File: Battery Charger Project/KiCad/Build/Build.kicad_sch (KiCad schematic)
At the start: 21 parts, among them J1 Screw_Terminal_01x03, J2 Screw_Terminal_01x03, J3 Screw_Terminal_01x02, J5 726386-2, J6 726386-2, J9 726386-2, U1 LAUNCHXL-F28379D, U2 TMCS1133C3A

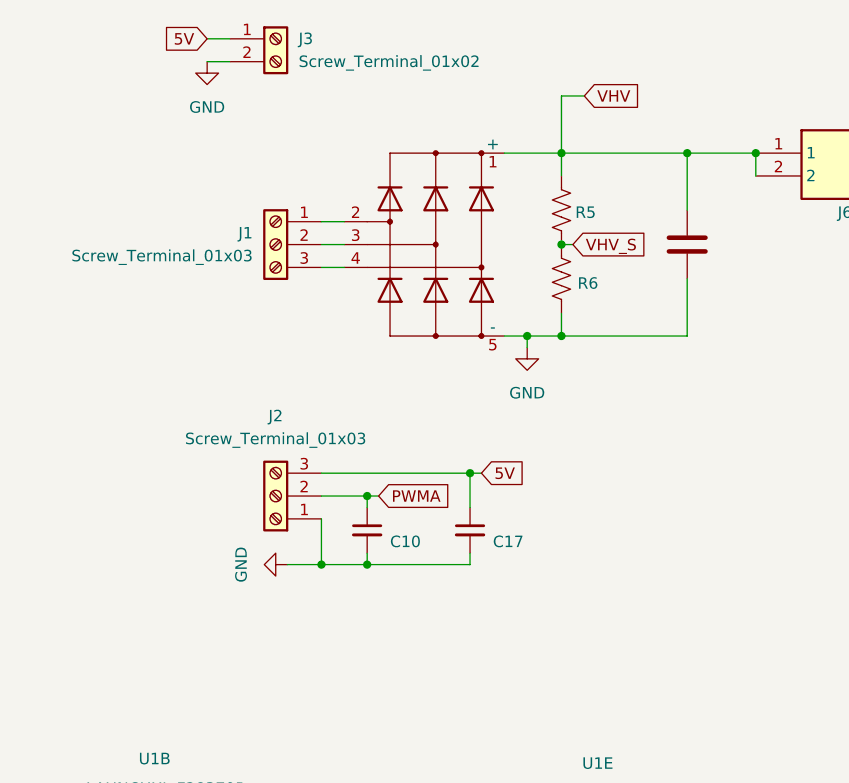
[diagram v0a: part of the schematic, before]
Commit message: Schematic updates
I sized the voltage divider resistors and began assigning footprints. I switched the generator connector for a new one that had a footprint in ultra librarian. It can also handle a higher current and voltage.
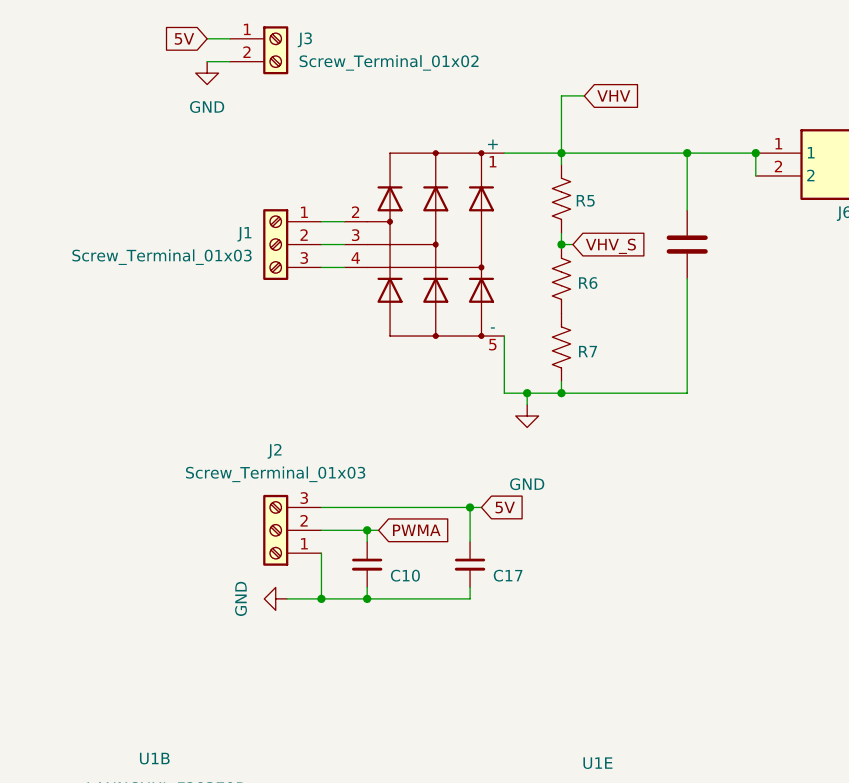
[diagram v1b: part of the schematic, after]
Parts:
- added R7: 69.8, Resistor_SMD:R_2010_5025Metric, symbol Device:R_US
- J3: footprint (none) -> 284391-2:CONN2_284391-2_TEC
- J5, J6, J9: footprint KiCad:726386-2 -> 284391-2:CONN2_284391-2_TEC
- R16: value R_Small_US -> 5K
- R17: value R_Small_US -> 680
- R5: value R_US -> 30K
- R6: value R_US -> 583
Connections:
- net GND: now also R7.2; no longer R6.2
- new net: R6.2, R7.1
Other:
- moved on the sheet: C10, C17, J2, R5

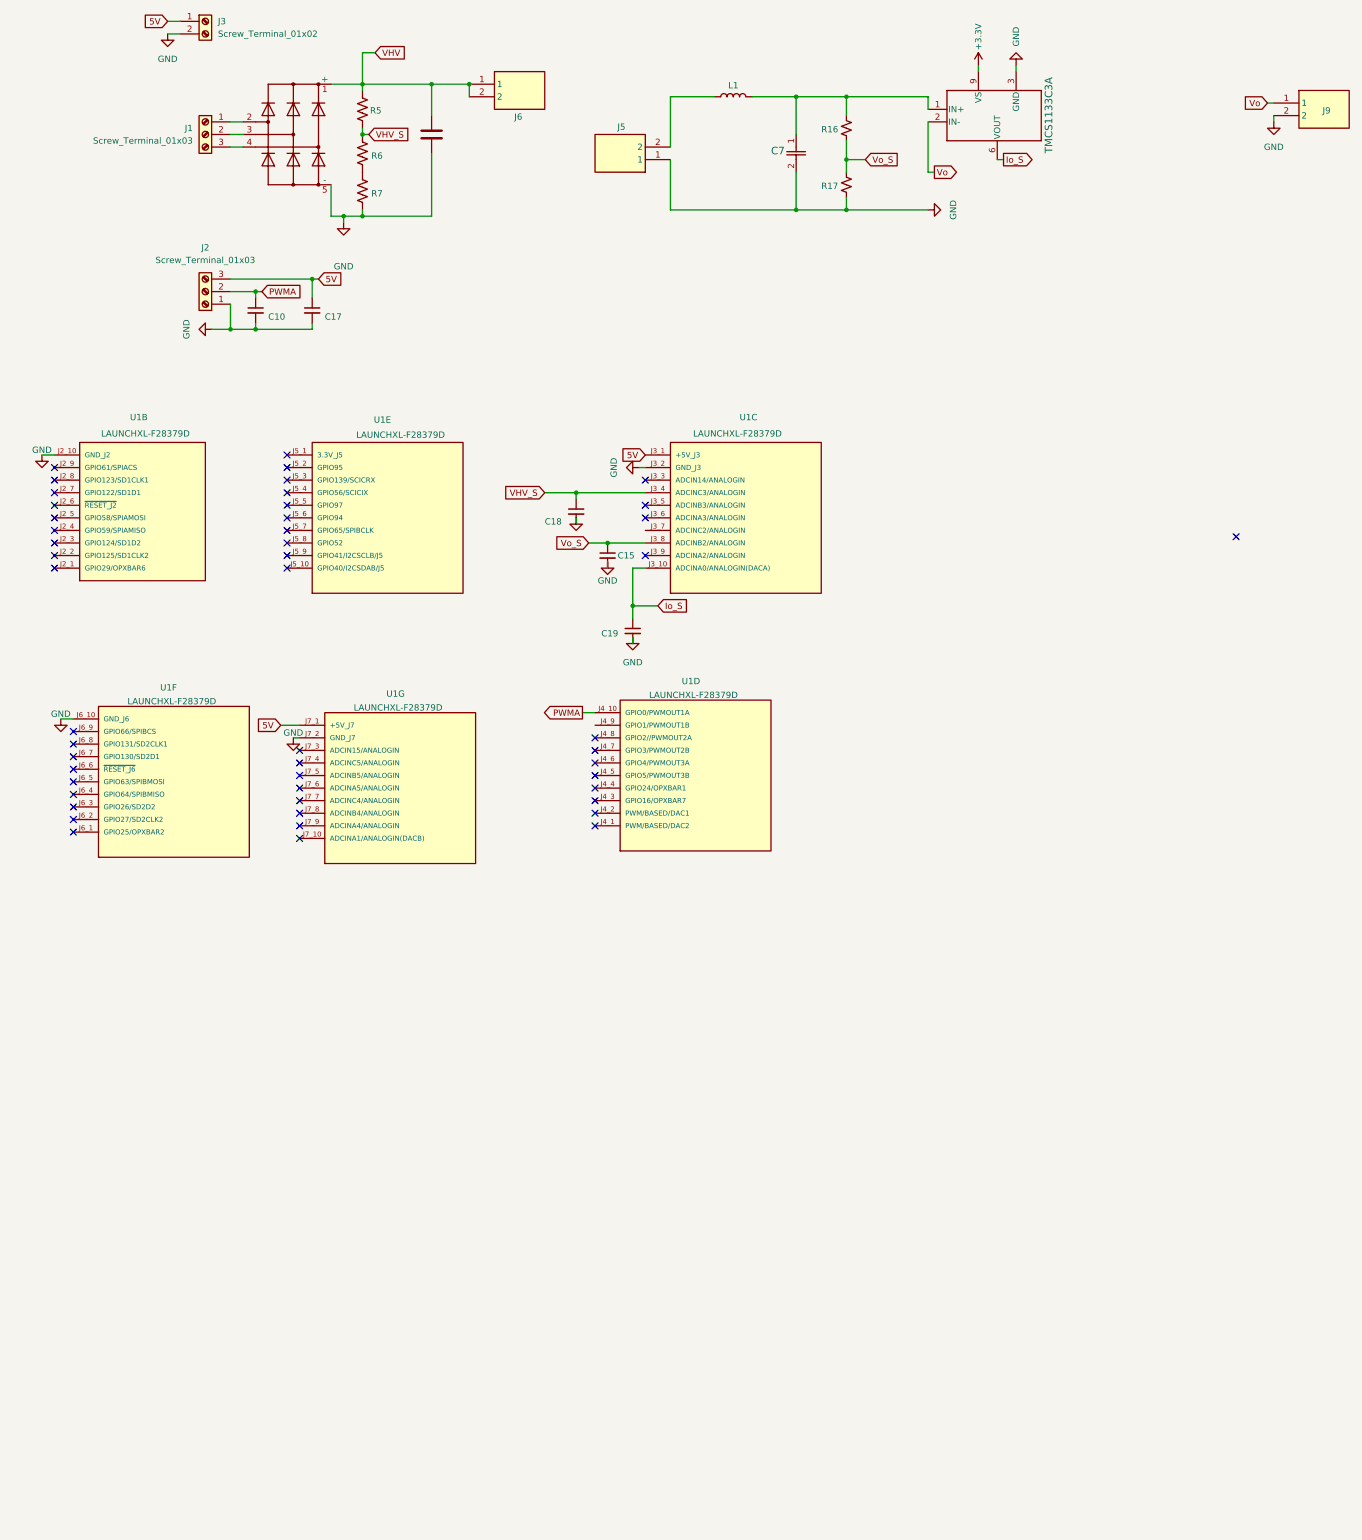
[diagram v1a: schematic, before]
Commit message: Made presentation and added footprintst
I finished the presentation. This required me to remove some things from the simulation to make it more understandable. I also just about finished adding all the footprints for the PCB
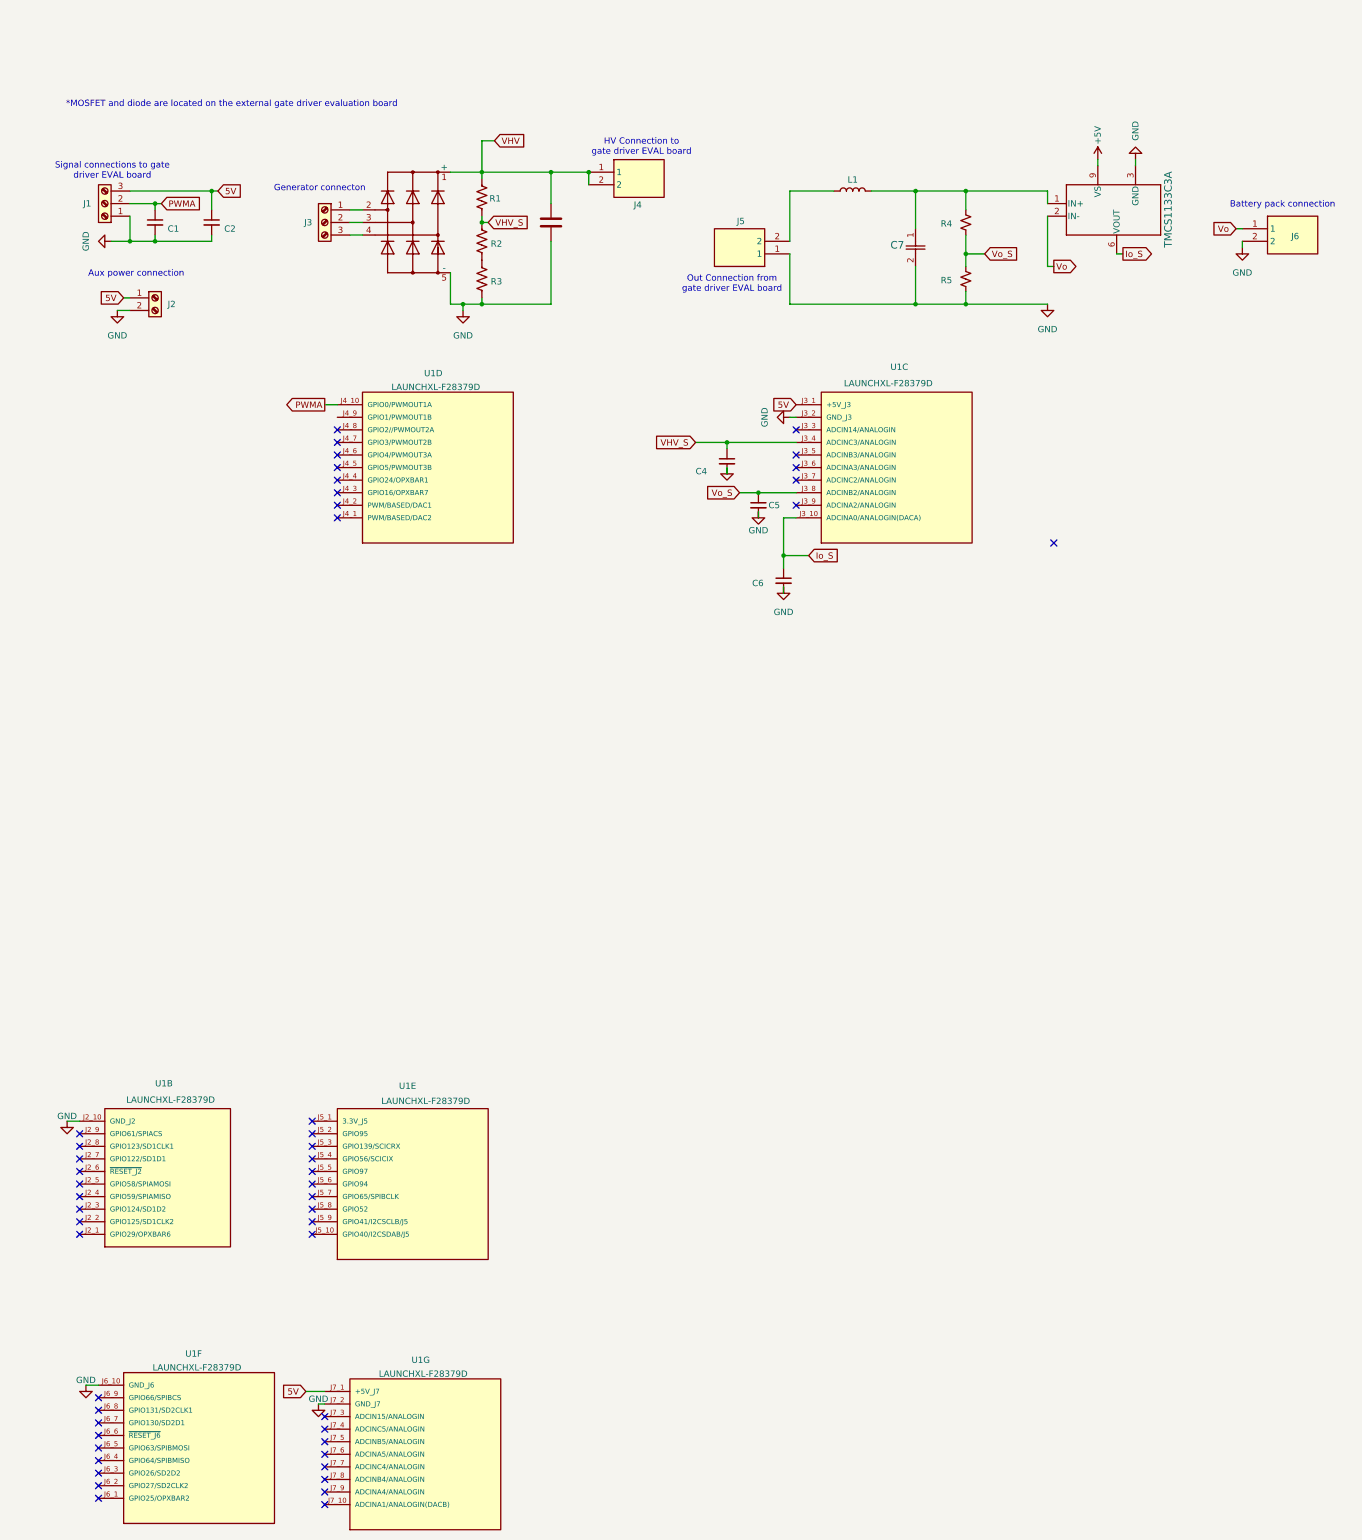
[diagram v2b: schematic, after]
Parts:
- J1: renamed from J2; footprint (none) -> 284391-3:CONN3_284391-3_TEC
- J3: renamed from J1; footprint (none) -> 277-1578-ND:CONN_1935174_PXC
- renumbered C10 to C1, C17 to C2, C2 to C3, C18 to C4, C15 to C5, C19 to C6, J3 to J2, J6 to J4, J9 to J6, R5 to R1, R6 to R2, R7 to R3, R16 to R4, R17 to R5
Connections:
- net +3.3V renamed +5V
- no-connect marks 49 -> 50
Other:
- note added: "*MOSFET and diode are located on the external gate driver evaluation board"
- note added: "Aux power connection"
- note added: "Battery pack connection"
- note added: "Generator connecton"
- note added: "HV Connection to gate driver EVAL board"
- note added: "Out Connection from gate driver EVAL board"
- note added: "Signal connections to gate driver EVAL board"
- moved on the sheet: C1, C2, C4, C5, C6, C7, J1, J2, J3, J4, J5, J6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

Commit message: More updates on PCB design
I forgot to push my changes for the last week, but I layed out the components and began routing traces and copper pours.
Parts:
- added C10, C8, C9: (no value), LGW2D561MELA30:CAP_A30_NCH, symbol Device:C
- added R6: 680, Resistor_SMD:R_2010_5025Metric, symbol Device:R_Small_US
- C3: footprint (none) -> LGW2D561MELA30:CAP_A30_NCH
- C7: footprint footprints:CAP_C45_NCH -> EEU-FR1H100:CAP_PAN_5X11_PAN
- D1: footprint Diode_THT:Diode_Bridge_IXYS_GUFP -> DPF30U200FC:DPF30U200FC
- L1: footprint Library:inductor_customized_v1 -> LC200-0185:LC200-0185
- R1: value 30K -> 300K
- R2: value 583 -> 6490
- R3: value 69.8 -> 36
- U1: footprint Library:MOD_LAUNCHXL-F28379D_v2 -> LAUNCHXL-F28379D:LAUNCHXL-F28379D
- U2: footprint DVG0010A_PMCS1133A1AQDVGR_TEX -> TMCS1133C5AQDVGR:TMCS1133C5AQDVGR
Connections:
- net GND: now also D1.2 (-), J4.2, J6.1, C10.2, C8.2, C9.2; no longer D1.5 (-), J5.1, J6.2
- net VHV: now also C10.1, C8.1, C9.1; no longer J4.2
- net Vo: now also J6.2; no longer J6.1
- net Vo_S: now also R6.1; no longer R5.1
- net at J5.2, L1.1: now also J5.1
- net A: now reaches J3.1 (Pin_1)
- net A: now also D1.3; no longer D1.2
- net B: now reaches J3.2 (Pin_2)
- net B: now also D1.4; no longer D1.3
- net C: now reaches J3.3 (Pin_3)
- net C: now also D1.5; no longer D1.4
- new net: R5.1, R6.2
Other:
- note added: "HV and GND Connection to gate driver EVAL board"
- note removed: "HV Connection to gate driver EVAL board"
- moved on the sheet: C4, C5, C6, C7, J4, J5, J6, L1, R4, R5, U1B, U1C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
